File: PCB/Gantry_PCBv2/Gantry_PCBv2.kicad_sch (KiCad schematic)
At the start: 151 parts, among them J1 Screw_Terminal_01x02, J10 B2B-XH-A_LF__SN_, J11 USB_C_Receptacle_USB2.0_16P, J12 Conn_01x04_Pin, J13 Conn_01x04_Pin, J14 Conn_01x04_Pin, J15 Conn_01x04_Pin, J16 Conn_01x05_Pin, J17 Conn_01x05_Pin, J2 DCJ200-10-A-XX-X_REVA, J3 Conn_01x03_Pin, J4 Conn_01x14, J5 B2B-XH-A_LF__SN_, J6 B2B-XH-A_LF__SN_, J7 B2B-XH-A_LF__SN_, J8 Conn_01x14, J9 Conn_01x10, Q1 NMOS, Q2 SS8050, Q3 SS8050, SW1 SW_0, SW2 SW_EN, SW3 SW_Push_DPDT, SW4 SW_Push_DPDT, U1 ESP32-WROOM-32E, U10 74HC245, U11 74HC245, U12 MCP23017_SO, U2 MP1584, U3 CH340C, U4 TLV75733PDBV, U5 DRV8825_STEPPER_MOTOR_DRIVER_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, U6 DRV8825_STEPPER_MOTOR_DRIVER_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, U7 TB6612FNG H-bridge Motor Driv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, U8 DRV8825_STEPPER_MOTOR_DRIVER_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, U9 DRV8825_STEPPER_MOTOR_DRIVER_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

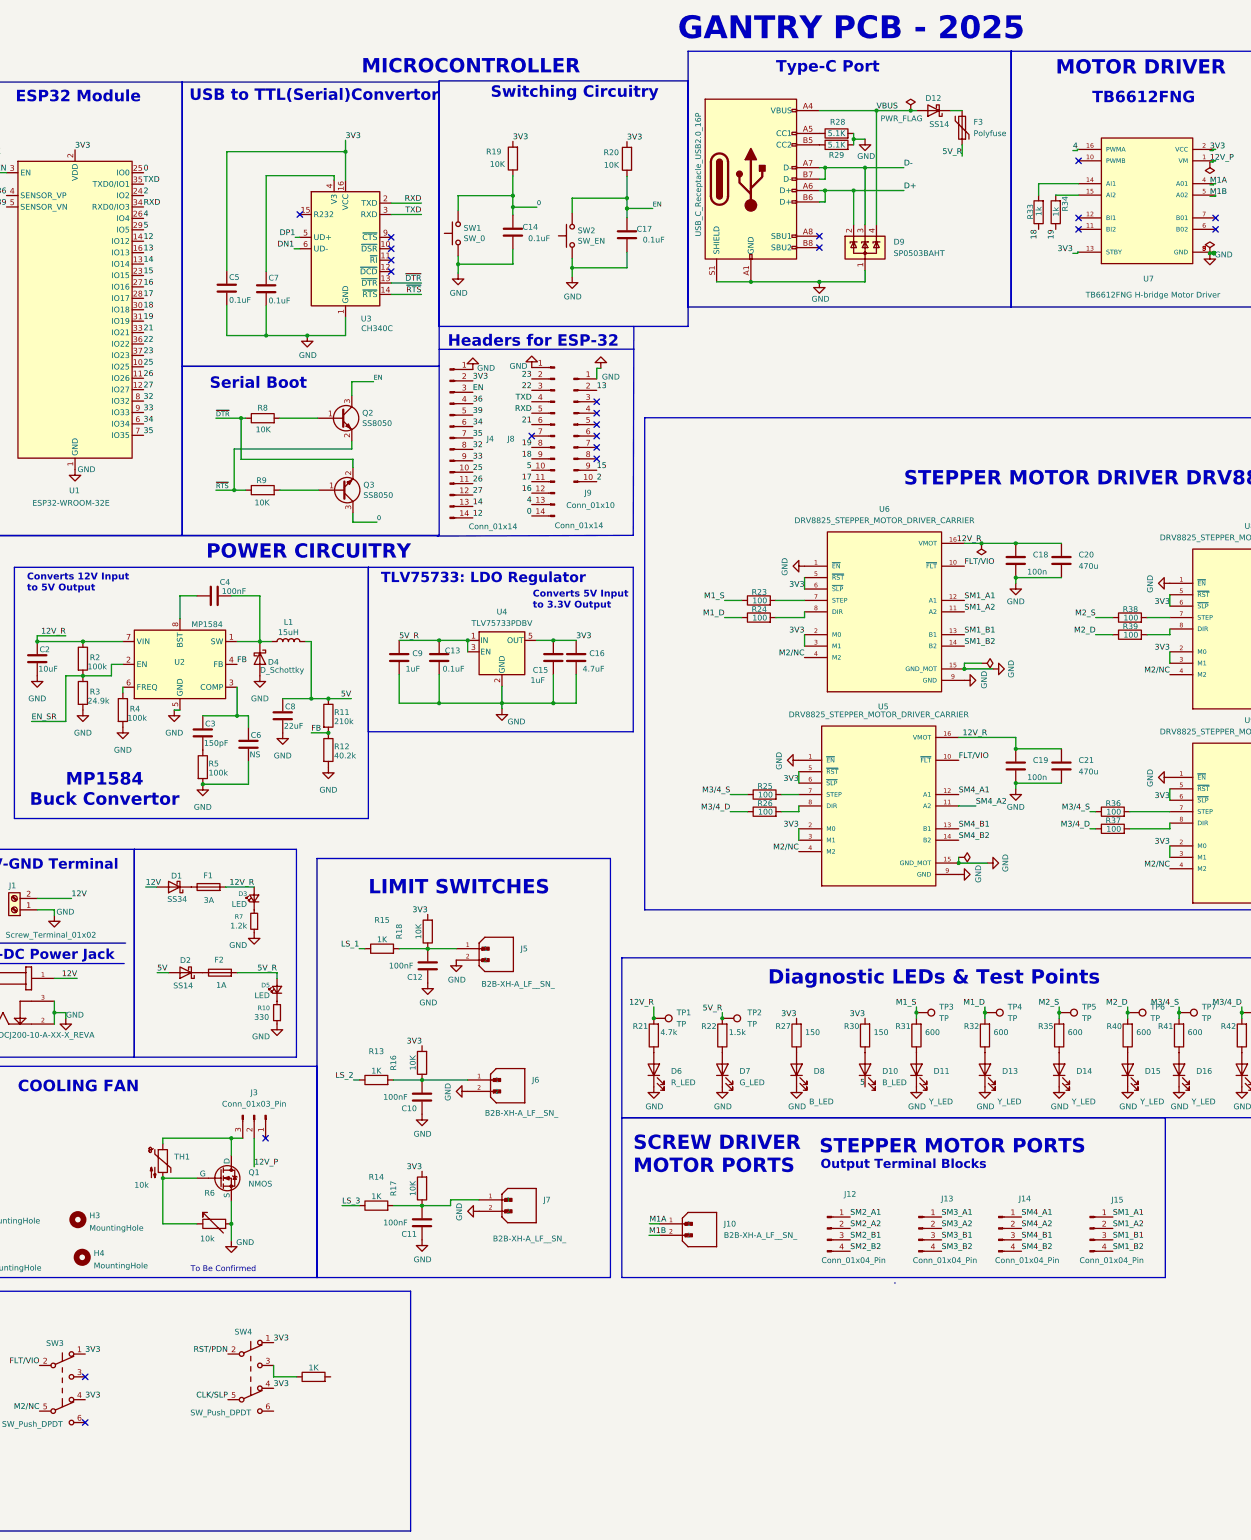
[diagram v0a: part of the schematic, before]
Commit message: Corrections in TMC2208 Integration(In Progress)
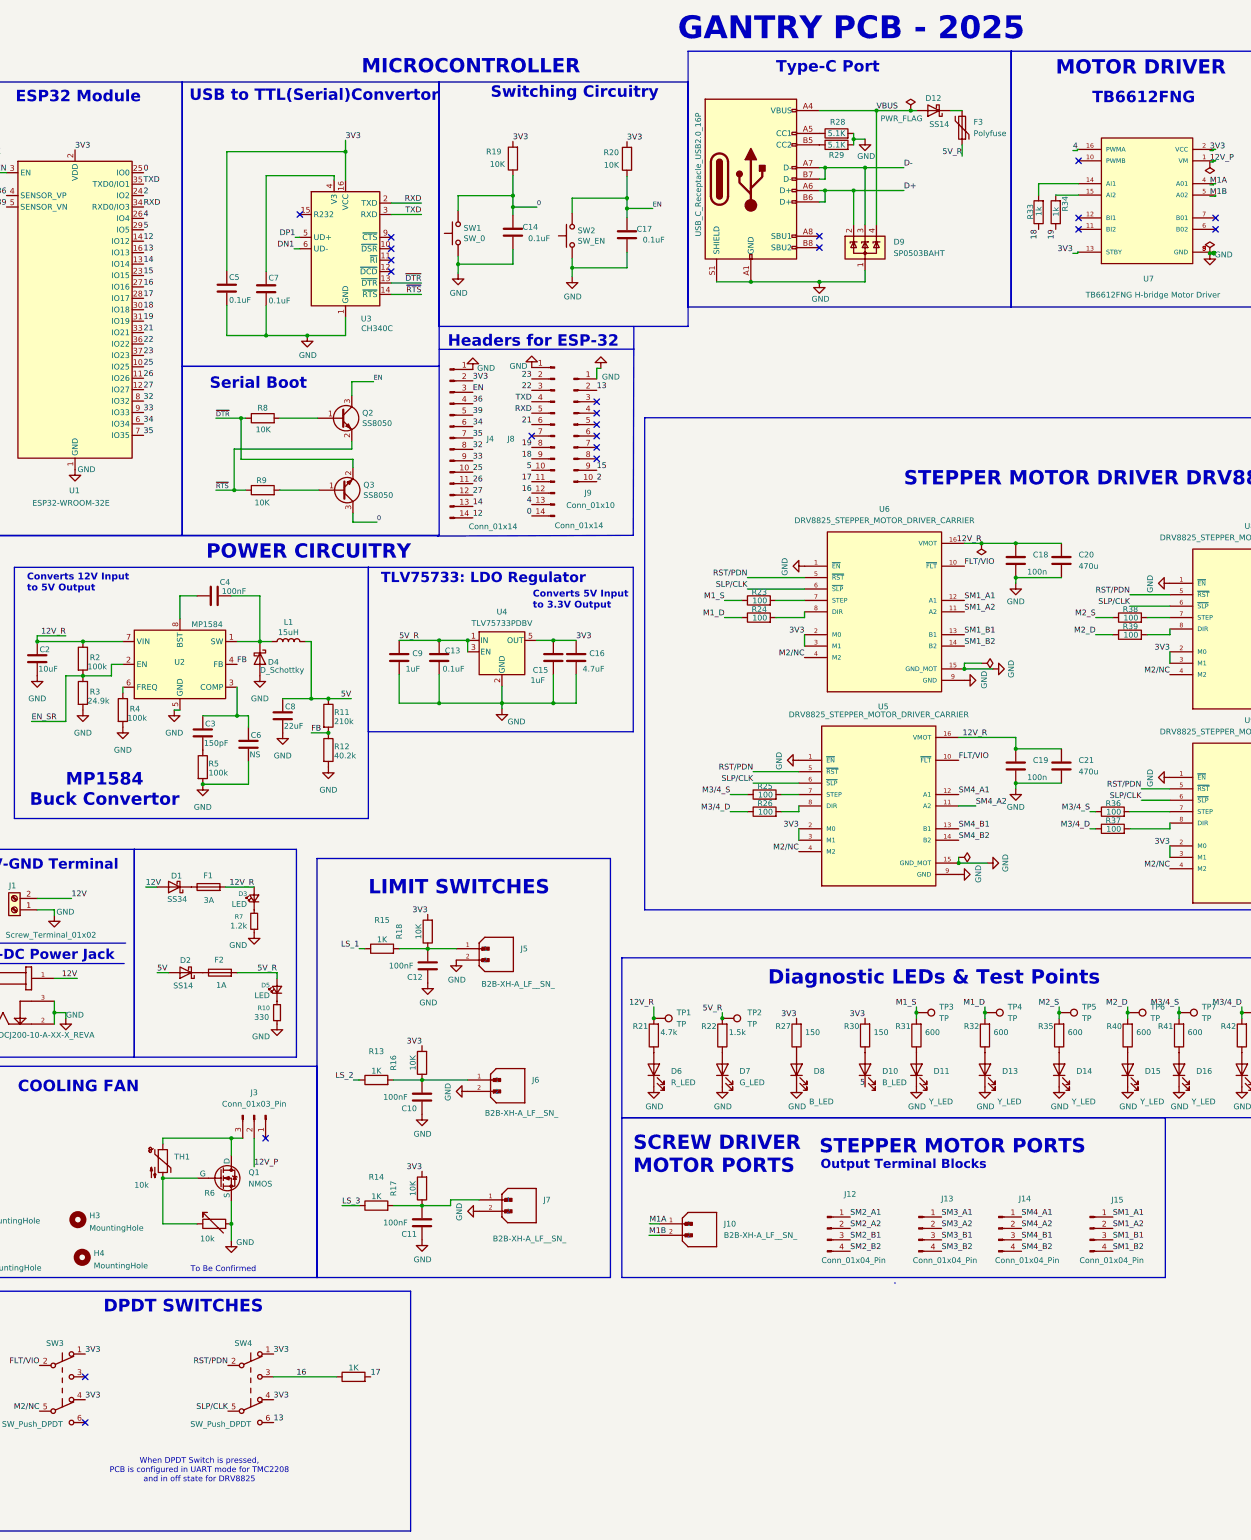
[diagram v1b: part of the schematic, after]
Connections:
- net 13: now also SW4.6 (C)
- net 16: now also R49.1, SW4.3 (C)
- net 17: now also R49.2
- net 3V3: no longer U5.5 (~{RST}), U5.6 (~{SLP}), U6.5 (~{RST}), U6.6 (~{SLP}), U8.5 (~{RST}), U8.6 (~{SLP}), U9.5 (~{RST}), U9.6 (~{SLP})
- net RST/PDN: now also U5.5 (~{RST}), U6.5 (~{RST}), U8.5 (~{RST}), U9.5 (~{RST})
- net CLK/SLP renamed SLP/CLK
- net SLP/CLK: now also U5.6 (~{SLP}), U6.6 (~{SLP}), U8.6 (~{SLP}), U9.6 (~{SLP})
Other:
- note added: "DPDT SWITCHES"
- note added: "When DPDT Switch is pressed, PCB is configured in UART mode for TMC2208 and in off state for DRV8825"
- moved on the sheet: SW4

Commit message: Fixed Cooling Fan Circuit, Changes in GPIO Expander
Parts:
- added C29: 10uF, Capacitor_SMD:C_0805_2012Metric_Pad1.18x1.45mm_HandSolder, symbol Device:C
- added C30: 0.1uF, Capacitor_SMD:C_0805_2012Metric_Pad1.18x1.45mm_HandSolder, symbol Device:C
- added JP1, JP2, JP3: SolderJumper, symbol Jumper:SolderJumper_2_Open
- added R50, R51: 10k, Resistor_SMD:R_0805_2012Metric_Pad1.20x1.40mm_HandSolder, symbol Device:R
- C1, C13, C14, C15, C16, C17, C2, C3, C4, C5, C6, C7, C8, C9: footprint Capacitor_SMD:C_0805_2012Metric -> Capacitor_SMD:C_0805_2012Metric_Pad1.18x1.45mm_HandSolder
- C10: value 100nF -> 0.1uF; footprint Capacitor_SMD:C_0805_2012Metric -> Capacitor_SMD:C_0805_2012Metric_Pad1.18x1.45mm_HandSolder
- C11, C12: value 100nF -> 0.1uF; footprint Capacitor_SMD:C_01005_0402Metric -> Capacitor_SMD:C_0805_2012Metric_Pad1.18x1.45mm_HandSolder
- C18, C19, C22, C23, C24, C27: value 100n -> 0.1uF; footprint Capacitor_SMD:CP_Elec_6.3x7.7 -> Capacitor_SMD:C_0805_2012Metric_Pad1.18x1.45mm_HandSolder
- C20, C21, C25, C26: value 470u -> 470uF; footprint Capacitor_SMD:CP_Elec_6.3x7.7 -> Capacitor_SMD:CP_Elec_10x10.5
- C28: value 100n -> 10uF; footprint Capacitor_SMD:CP_Elec_6.3x7.7 -> Capacitor_SMD:C_0805_2012Metric_Pad1.18x1.45mm_HandSolder
- R1, R19, R20, R21, R22, R27, R30, R31, R32, R35, R40, R41, R42, R8, R9: footprint Resistor_SMD:R_0805_2012Metric -> Resistor_SMD:R_0805_2012Metric_Pad1.20x1.40mm_HandSolder
- R10: footprint Resistor_SMD:R_0603_1608Metric_Pad0.98x0.95mm_HandSolder -> Resistor_SMD:R_0805_2012Metric_Pad1.20x1.40mm_HandSolder
- R23, R24, R25, R26, R33, R34, R36, R37, R38, R39: footprint Resistor_SMD:R_0603_1608Metric -> Resistor_SMD:R_0805_2012Metric_Pad1.20x1.40mm_HandSolder
- R43, R44, R45, R46, R47, R48: value 100k -> 10k
- R6: footprint Resistor_SMD:R_0815_2038Metric -> Resistor_SMD:R_0805_2012Metric_Pad1.20x1.40mm_HandSolder
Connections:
- net 12V_P: now also TH1.1
- net 21: now also R50.1
- net 22: now also R51.1
- net 3V3: now also R44.1, R48.1, C29.1, C30.1, JP1.2 (B), JP2.2 (B), JP3.2 (B), R50.2, R51.2; no longer R44.2, R45.2, R46.2, R47.2, R48.2, U12.15 (A0), U12.16 (A1), U12.17 (A2)
- net GND: now also C29.2, C30.2
- net at U12.18 (~{RESET}): now also R48.2; no longer R48.1
- net at J3.3 (Pin_3), Q1.1 (D): no longer TH1.1
- net at U12.20 (INTA): now also R44.2; no longer R44.1
- new net: JP2.1 (A), R46.2, U12.16 (A1)
- new net: JP1.1 (A), R45.2, U12.15 (A0)
- new net: JP3.1 (A), R47.2, U12.17 (A2)
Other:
- note added: "A0, A1, and A2 are address pins for the I/O expander. Since only one device is currently used, these pins are grounded by default. Solder jumpers are provided to allow the pins to be disconnected from GND and tied HIGH if multiple modules are added in the future, enabling address reconfiguration."
- moved on the sheet: C28, J3, Q1, R43, R44, R45, R46, R47, R48, R6, TH1

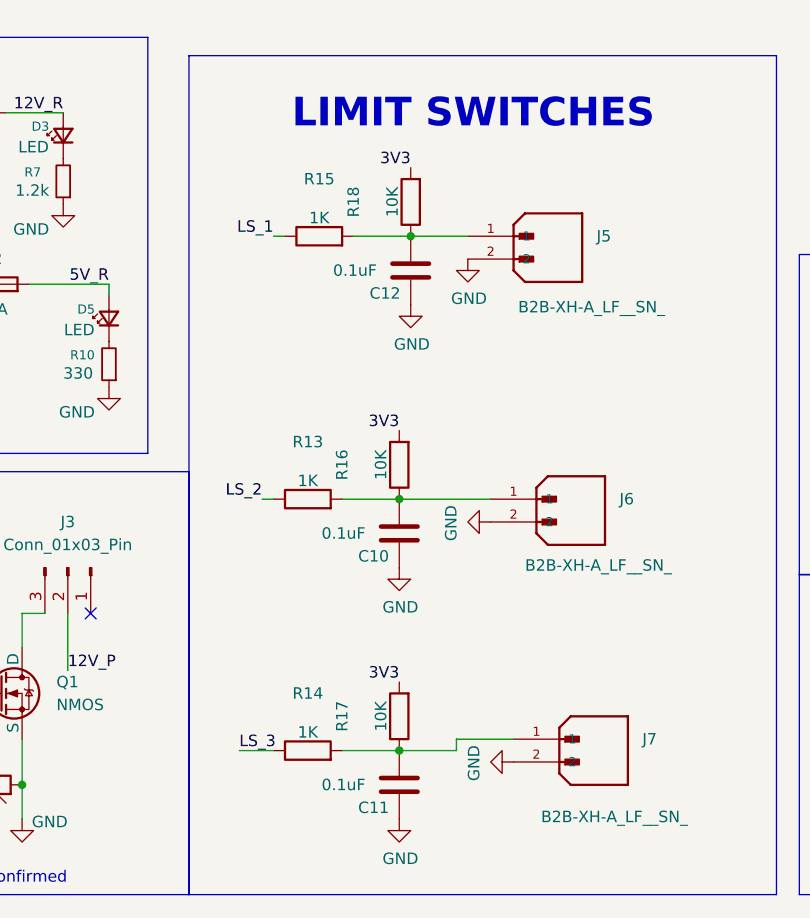
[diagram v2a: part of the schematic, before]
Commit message: Added Solder Jumper Footprint and DNPed 10K limit switch resistor
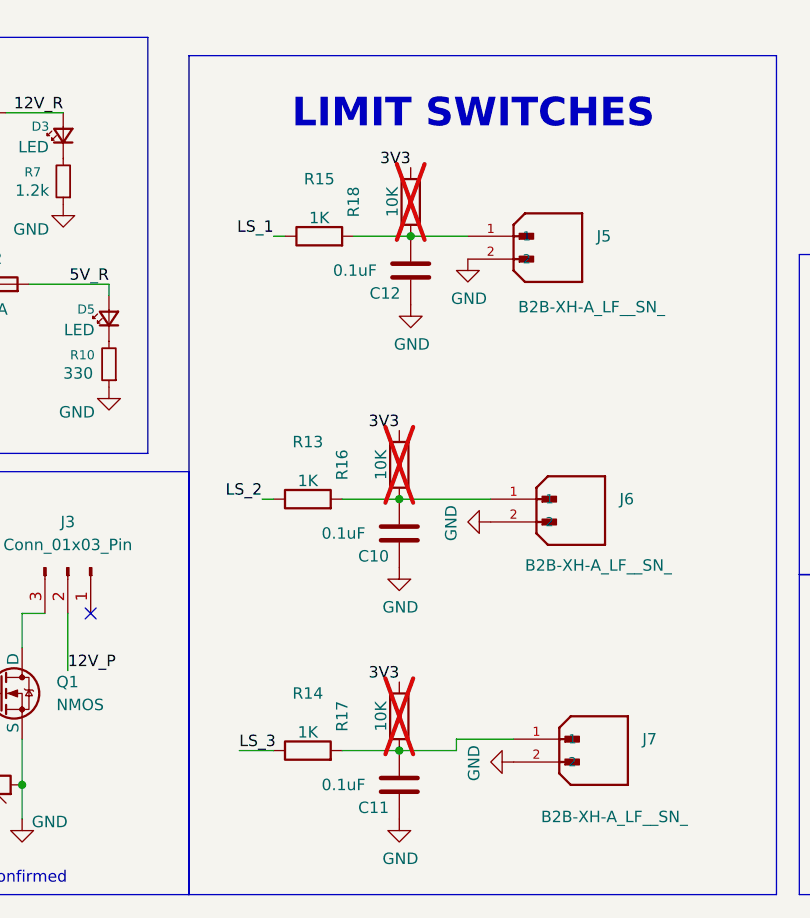
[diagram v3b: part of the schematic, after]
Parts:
- JP1, JP2, JP3: footprint (none) -> Jumper:SolderJumper-3_P1.3mm_Open_Pad1.0x1.5mm_NumberLabels
- R16, R17, R18: DNP (none) -> Yes; now not fitted
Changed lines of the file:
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@@
 		(in_bom yes)
 		(on_board yes)
-		(dnp no)
+		(dnp yes)
 		(property "Reference" "R16"
 			(at 107.95 236.22 90)
@@
 			)
 		)
+		(property "DNP" "Yes"
+			(at 114.3 236.22 90)
+			(effects
+				(font
+					(size 1.27 1.27)
+				)
+				(hide yes)
+			)
+		)
 		(pin "1"
 		)
@@
 		(in_bom yes)
 		(on_board yes)
-		(dnp no)
+		(dnp yes)
 		(property "Reference" "R18"
 			(at 109.22 207.01 90)
@@
 			)
 		)
+		(property "DNP" "Yes"
+			(at 115.57 207.01 90)
+			(effects
+				(font
+					(size 1.27 1.27)
+				)
+				(hide yes)
+			)
+		)
 		(pin "1"
 		)
@@
 			)
 		)
-		(property "Footprint" ""
+		(property "Footprint" "Jumper:SolderJumper-3_P1.3mm_Open_Pad1.0x1.5mm_NumberLabels"
 			(at 359.41 256.54 0)
 			(effects
@@
 		(in_bom yes)
 		(on_board yes)
-		(dnp no)
+		(dnp yes)
 		(property "Reference" "R17"
 			(at 107.95 264.16 90)
@@
 			)
 		)
+		(property "DNP" "Yes"
+			(at 114.3 264.16 90)
+			(effects
+				(font
+					(size 1.27 1.27)
+				)
+				(hide yes)
+			)
+		)
 		(pin "1"
 		)
@@
 			)
 		)
-		(property "Footprint" ""
+		(property "Footprint" "Jumper:SolderJumper-3_P1.3mm_Open_Pad1.0x1.5mm_NumberLabels"
 			(at 369.57 256.54 0)
 			(effects
@@
 			)
 		)
-		(property "Footprint" ""
+		(property "Footprint" "Jumper:SolderJumper-3_P1.3mm_Open_Pad1.0x1.5mm_NumberLabels"
 			(at 351.79 256.54 0)
 			(effects
